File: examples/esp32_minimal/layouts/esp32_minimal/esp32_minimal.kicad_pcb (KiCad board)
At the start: 2 copper layers, 34.2 x 26.8 mm, 17 parts

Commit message: update esp32minimal to latest packages
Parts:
- removed R10, R11: 4.7kΩ ±1% 62.5mW, UNI_ROYAL_0402WGF4701TCE:R0402
- added C3: 100nF ±10% 16V X7R, Samsung_Electro_Mechanics_CL05B104KO5NNNC:C0402, F.Cu at (12.2, -6.50)
- added D1: , STMicroelectronics_USBLC6_2SC6:SOT-23-6_L2.9-W1.6-P0.95-LS2.8-BL, F.Cu at (10.0, -5.75)
- added F1: , BHFUSE_BSMD0805_050_15V:F0805, F.Cu at (6.00, -5.50)
- added R6: 5.1kΩ ±1% 62.5mW, UNI_ROYAL_0402WGF5101TCE:R0402, F.Cu at (7.75, -5.75)
- added R7: 5.1kΩ ±1% 62.5mW, UNI_ROYAL_0402WGF5101TCE:R0402, F.Cu at (13.5, -5.75)
- C9: value 22µF ±20% 6.3V X5R -> 22µF ±20% 25V X5R; footprint Samsung_Electro_Mechanics_CL21A226MQQNNNE:C0805 -> Samsung_Electro_Mechanics_CL21A226MAQNNNE:C0805
- USB1: footprint kinghelm_KH_TYPE_C_16P:USB-C-SMD_KH-TYPE-C-16P -> SHOU_HAN_TYPE_C_16PIN_2MD_073:USB-C-SMD_TYPE-C-6PIN-2MD-073
- moved USB1 183.7 mm to (10.0, 0.00)
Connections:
- net -hv-1 renamed power-VCC
- net FB renamed VDIV_OUTPUT
- net input-0 renamed button-input-input-0
- net input-1 renamed button-input-input-1
- net micro-line-0 renamed gpios[10]-line
- net micro-line-1 renamed MOSI
- net micro-line-10 renamed TX
- net micro-line-11 renamed i2s[0]-SCK
- net micro-line-12 renamed TCK
- net micro-line-13 renamed gpios[3]-WS
- net micro-line-14 renamed TDO
- net micro-line-15 renamed TDI
- net micro-line-16 renamed TMS
- net micro-line-17 renamed gpios[4]-SD
- net micro-line-18 renamed gpios[5]-SCK
- net micro-line-19 renamed i2s[1]-WS
- net micro-line-2 renamed gpios[12]-SCLK
- net micro-line-20 renamed gpios[7]-SDA
- net micro-line-21 renamed i2s[1]-SD
- net micro-line-3 renamed spi[2]-MISO
- net micro-line-4 renamed gpios[14]-SCL
- net micro-line-5 renamed spi[3]-SDA
- net micro-line-6 renamed gpios[16]-SCLK
- net micro-line-7 renamed spi[3]-MISO
- net micro-line-8 renamed RX
- net micro-line-9 renamed gpios[1]-SCL
- net output-0 renamed gpios[0]-output
- net output-1 renamed enable-output
- C1 pad 1: -hv-0 -> power_in-VCC
- C1 pad 2: gnd -> GND
- C10 pad 2: gnd -> GND
- C2 pad 2: gnd -> GND
- C8 pad 2: gnd -> GND
- C9 pad 2: gnd -> GND
- R1 pad 2: gnd -> GND
- R2 pad 2: gnd -> GND
- R4 pad 2: gnd -> GND
- U2 pad 1: gnd -> GND
- U2 pad 13: -line-0 -> USB_D_N
- U2 pad 14: -line-1 -> USB_D_P
- U2 pad 40: gnd -> GND
- U2 pad 41: gnd -> GND
- U3 pad 3: gnd -> GND
- U3 pad 4: -hv-0 -> power_in-VCC
- U3 pad 6: -hv-0 -> power_in-VCC
- U3 pad 7: gnd -> GND
- USB1 pad 1: gnd -> (no net)
- USB1 pad 2: gnd -> power_vbus-VCC
- USB1 pad 3: gnd -> sbu[1]-line
- USB1 pad 4: gnd -> cc[0]-line
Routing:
- net (no net): track 1.14 -> 97.4 mm, vias 0 -> 18
- net gnd: track 41.9 -> 0.00 mm, vias 11 -> 0
- net -hv-0: track 21.6 -> 0.00 mm, vias 4 -> 0
- net -line-1: track 12.7 -> 0.00 mm
- net -line-0: track 12.6 -> 0.00 mm, vias 2 -> 0
- net power_vbus-VCC: track 0.00 -> 10.6 mm
- net power_in-VCC: track 0.00 -> 10.0 mm, vias 0 -> 3
- net USB_D_N: track 0.00 -> 7.57 mm
- net net: track 7.53 -> 0.00 mm, vias 1 -> 0
- net USB_D_P: track 0.00 -> 6.68 mm
- net GND: track 0.00 -> 3.85 mm, vias 0 -> 3
- net cc[1]-line: track 0.00 -> 3.66 mm
- net cc[0]-line: track 0.00 -> 3.35 mm
- net B5: track 1.65 -> 0.00 mm
- net A5: track 1.60 -> 0.00 mm
- added copper zone on B.Cu, net (none)
- added copper zone on F.Cu, net (none)
- added copper zone on B.Cu, net GND
- added copper zone on F.Cu, net GND
- removed copper zone on B.Cu, net gnd
- removed copper zone on F.Cu, net gnd

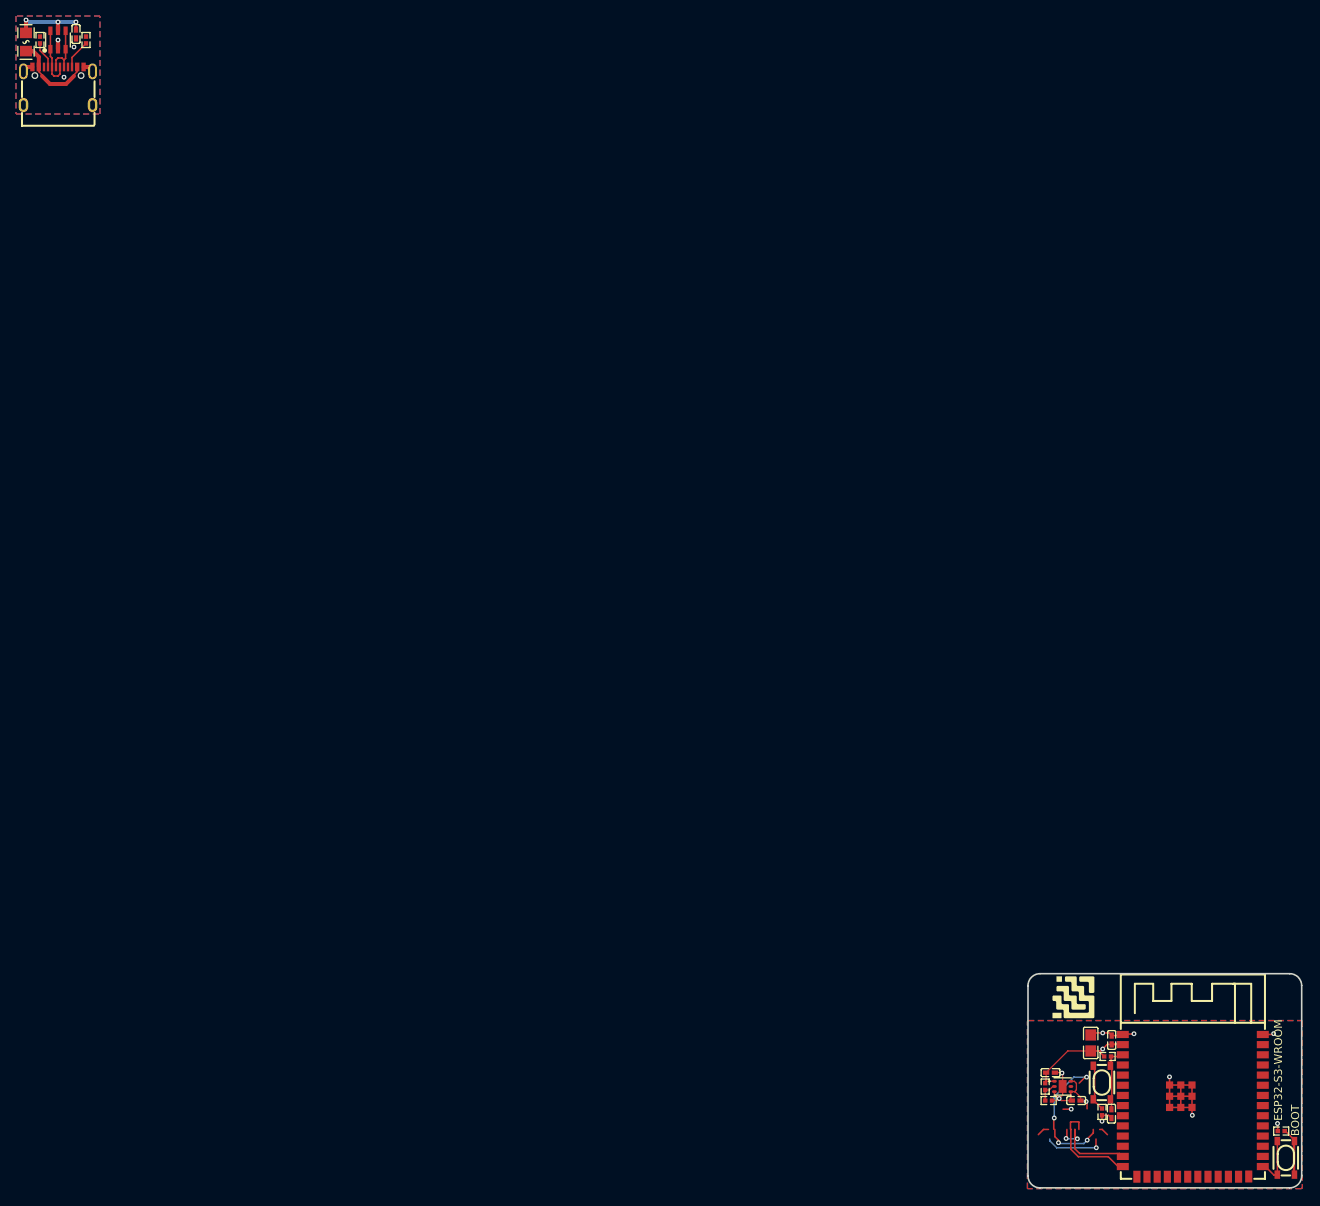
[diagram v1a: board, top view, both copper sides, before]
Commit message: minimal esp building with latest packages and compiler
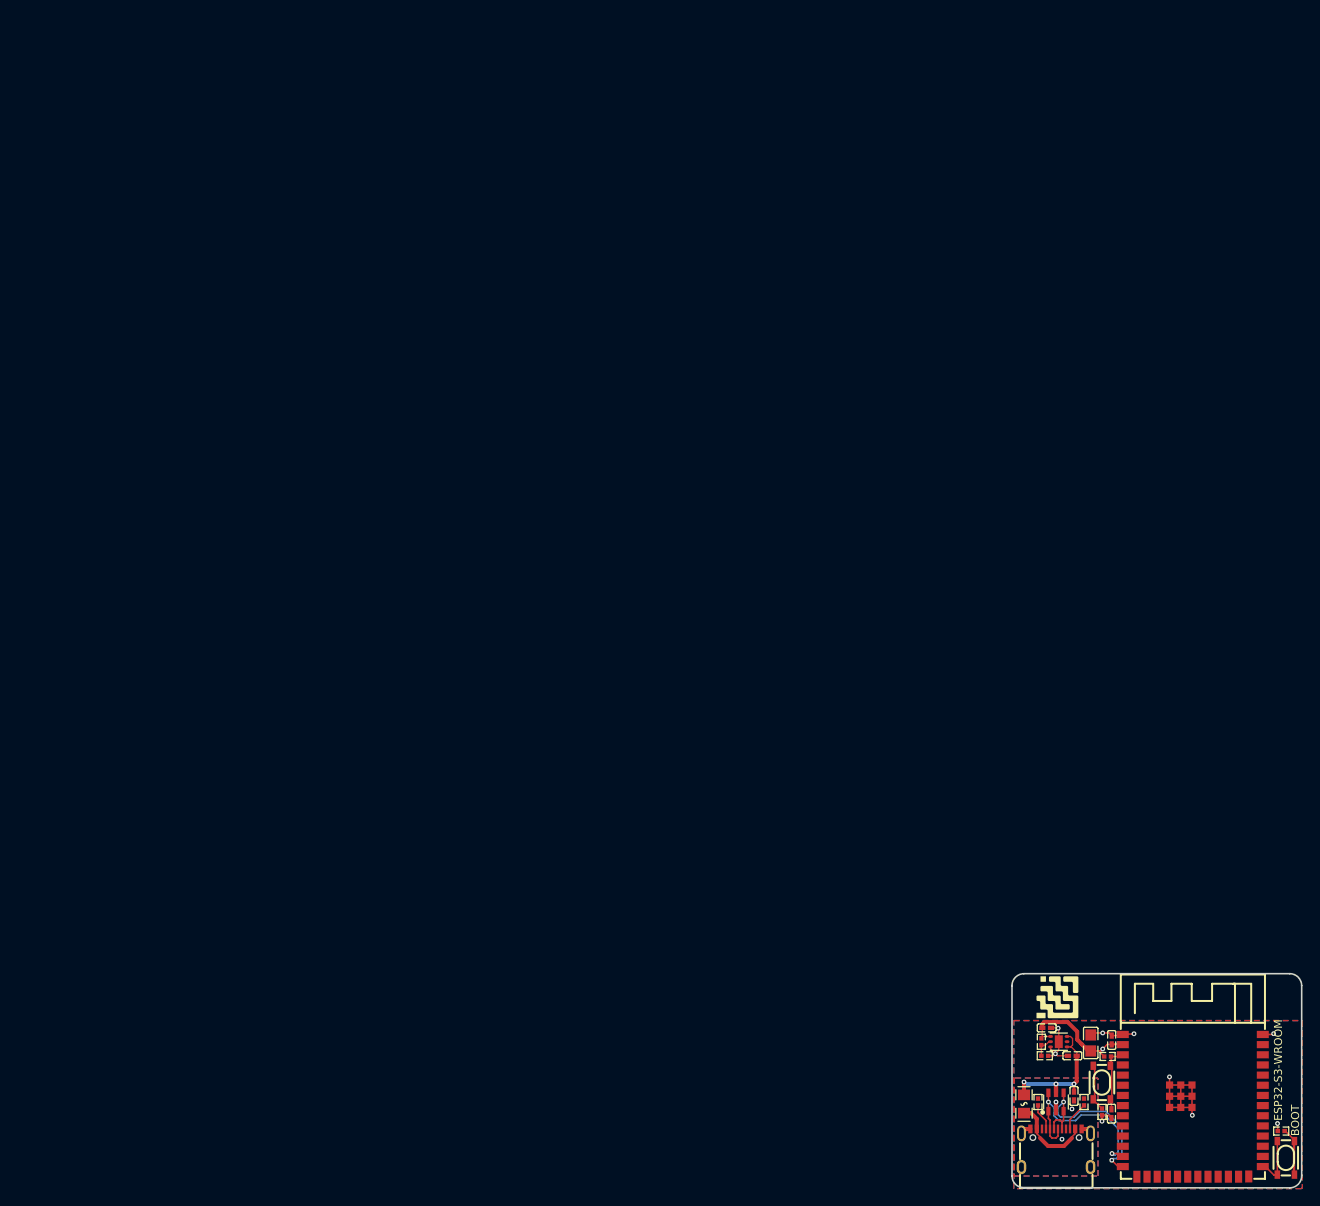
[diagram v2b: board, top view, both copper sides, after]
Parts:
- moved C3 182.2 mm to (137.0, 126.2)
- moved D1 182.2 mm to (134.8, 127.0)
- moved F1 182.2 mm to (130.8, 127.2)
- moved R6 182.2 mm to (132.5, 127.0)
- moved R7 182.2 mm to (138.2, 127.0)
- moved USB1 182.2 mm to (134.8, 132.8)
- moved U3 5.62 mm to (135.1, 119.5)
- moved C2 5.62 mm to (133.6, 117.7)
- moved C1 5.62 mm to (136.8, 121.2)
- moved R1 5.62 mm to (133.3, 121.2)
- moved R5 5.62 mm to (132.9, 119.5)
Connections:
- net gpios[1]-SCL renamed i2c[0]-SCL
- net i2s[0]-SCK renamed gpios[2]-SCK
- net i2s[1]-WS renamed gpios[6]-WS
- net spi[3]-SDA renamed uart[0]-SDA
- C3 pad 2: (no net) -> GND
- D1 pad 2: (no net) -> GND
- USB1 pad 1: (no net) -> GND
- USB1 pad 12: (no net) -> GND
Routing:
- net (no net): track 97.4 -> 0.00 mm, vias 18 -> 0
- net GND: track 3.85 -> 41.0 mm, vias 3 -> 12
- net USB_D_P: track 6.68 -> 24.2 mm, vias 0 -> 2
- net USB_D_N: track 7.57 -> 24.1 mm, vias 0 -> 2
- net power_in-VCC: track 10.0 -> 17.5 mm
- net power-VCC: track 16.1 -> 18.1 mm
- removed copper zone on B.Cu, net (none)
- removed copper zone on F.Cu, net (none)
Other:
- board size 34.2 x 26.8 mm -> 36.2 x 26.8 mm

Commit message: layout updates
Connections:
- net i2c[0]-SCL renamed gpios[1]-SCL
- net power-VCC renamed power_shim-VCC
- net uart[0]-SDA renamed spi[3]-SDA
- USB1 pad : net -> (no net)
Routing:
- net USB_D_P: track 24.2 -> 25.4 mm
- net USB_D_N: track 24.1 -> 25.3 mm

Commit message: lock net names with latest
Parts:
- C9: value 22µF ±20% 25V X5R -> 22µF ±20% 6.3V X5R; footprint Samsung_Electro_Mechanics_CL21A226MAQNNNE:C0805 -> Samsung_Electro_Mechanics_CL21A226MQQNNNE:C0805
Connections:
- net MOSI renamed spi[2]-MOSI
- net enable-output renamed output-output
- net gpios[10]-line renamed spi_cs[2]-line
- net gpios[12]-SCLK renamed SCLK
- net gpios[14]-SCL renamed spi_cs[3]-SCL
- net gpios[16]-SCLK renamed CTS
- net gpios[1]-SCL renamed i2c[0]-SCL
- net gpios[2]-SCK renamed i2s[0]-SCK
- net gpios[3]-WS renamed i2s[0]-WS
- net gpios[4]-SD renamed i2s[0]-SD
- net gpios[5]-SCK renamed i2s[1]-SCK
- net gpios[6]-WS renamed i2s[1]-WS
- net gpios[7]-SDA renamed SDA
- net power_shim-VCC renamed power-VCC
- net spi[3]-MISO renamed uart[1]-MISO
- net spi[3]-SDA renamed uart[0]-MOSI
- USB1 pad : (no net) -> net

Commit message: commit example parts
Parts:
- R1: value 10kΩ ±1% 62.5mW -> 2kΩ ±1% 62.5mW; footprint UNI_ROYAL_0402WGF1002TCE:R0402 -> UNI_ROYAL_0402WGF2001TCE:R0402
- R5: value 47kΩ ±1% 62.5mW -> 10kΩ ±1% 62.5mW; footprint UNI_ROYAL_0402WGF4702TCE:R0402 -> UNI_ROYAL_0402WGF1002TCE:R0402

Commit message: examples
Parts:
- R1: value 2kΩ ±1% 62.5mW -> 10kΩ ±1% 62.5mW; footprint UNI_ROYAL_0402WGF2001TCE:R0402 -> UNI_ROYAL_0402WGF1002TCE:R0402
- R5: value 10kΩ ±1% 62.5mW -> 47kΩ ±1% 62.5mW; footprint UNI_ROYAL_0402WGF1002TCE:R0402 -> UNI_ROYAL_0402WGF4702TCE:R0402
